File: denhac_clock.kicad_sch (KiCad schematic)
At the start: 54 parts, among them SW1 SET, SW2 CHANGE, U1 SN74HC595N, U2 D_H1, U3 SN74HC595N, U4 D_H1, U5 SN74HC595N, U6 D_M1, U7 SN74HC595N, U8 D_M2, U9 DS1307+, Y1 32.768kHz

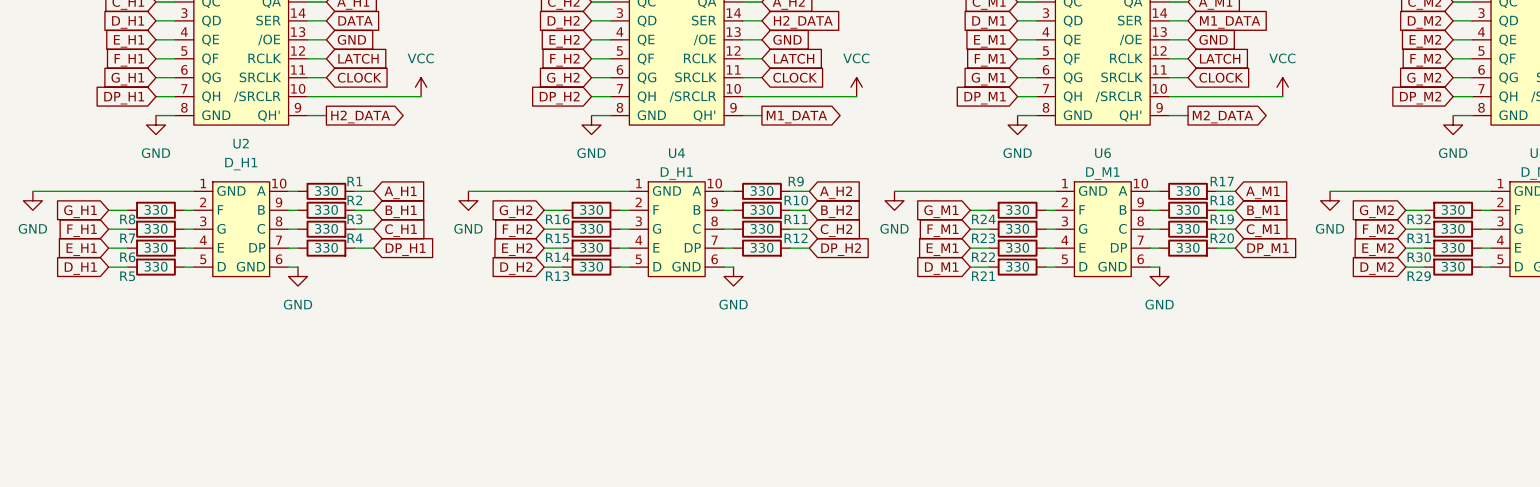
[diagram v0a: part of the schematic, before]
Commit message: rotate D_M1 by 180 degrees so that we can use D_H2 and D_M1 decimal points to create a "colon", and fix pins F and G on all D_ elements"
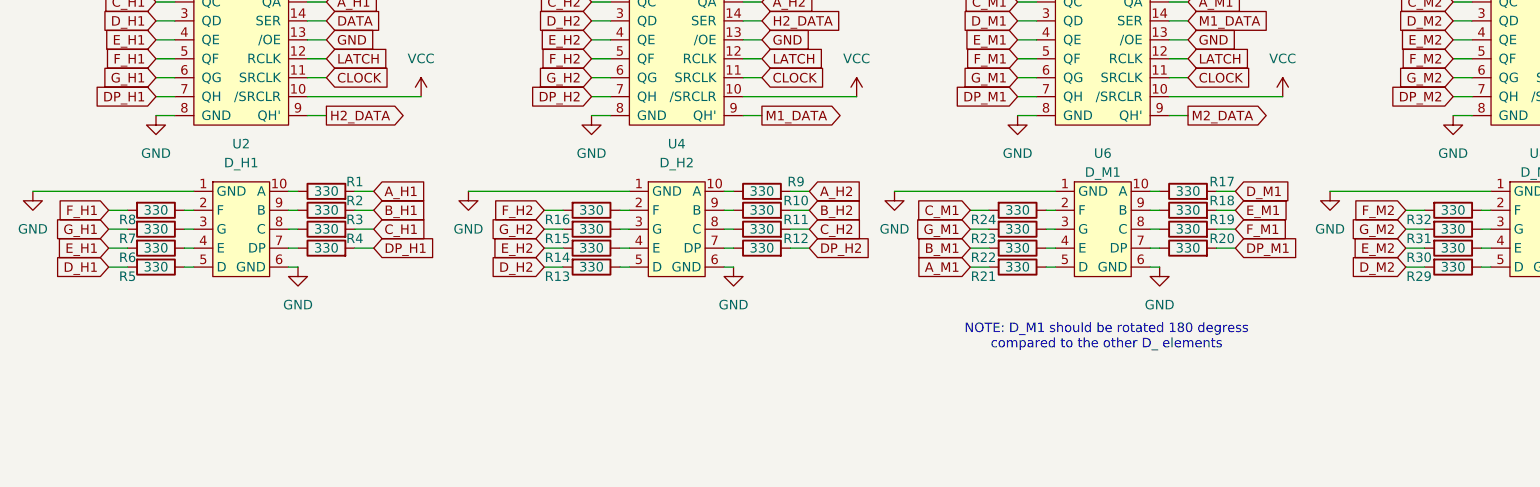
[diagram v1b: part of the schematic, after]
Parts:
- U4: value D_H1 -> D_H2
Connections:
- net A_M1: now also R21.2; no longer R17.2
- net B_M1: now also R22.2; no longer R18.2
- net C_M1: now also R24.2; no longer R19.2
- net D_M1: now also R17.2; no longer R21.2
- net E_M1: now also R18.2; no longer R22.2
- net F_H1: now also R8.2; no longer R7.2
- net F_H2: now also R16.2; no longer R15.2
- net F_M1: now also R19.2; no longer R23.2
- net F_M2: now also R32.2; no longer R31.2
- net G_H1: now also R7.2; no longer R8.2
- net G_H2: now also R15.2; no longer R16.2
- net G_M1: now also R23.2; no longer R24.2
- net G_M2: now also R31.2; no longer R32.2
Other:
- note added: "NOTE: D_M1 should be rotated 180 degress compared to the other D_ elements"
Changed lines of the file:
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@@
 	(generator_version "9.0")
 	(paper "A4")
+	(text "NOTE: D_M1 should be rotated 180 degress\ncompared to the other D_ elements"
+		(exclude_from_sim no)
+		(at 175.768 70.358 0)
+		(effects
+			(font
+				(size 1.27 1.27)
+			)
+		)
+	)
 	(junction
 		(at 62.23 179.07)
@@
 		)
 	)
-	(global_label "D_M1"
+	(global_label "A_M1"
 		(shape input)
 		(at 157.48 60.96 180)
@@
 		)
 		(property "Intersheetrefs" "${INTERSHEET_REFS}"
-			(at 149.5963 60.96 0)
+			(at 149.7777 60.96 0)
 			(effects
 				(font
@@
 		)
 	)
-	(global_label "A_M1"
+	(global_label "D_M1"
 		(shape input)
 		(at 193.04 50.8 0)
@@
 		)
 		(property "Intersheetrefs" "${INTERSHEET_REFS}"
-			(at 200.7423 50.8 0)
+			(at 200.9237 50.8 0)
 			(effects
 				(font
@@
 	(global_label "F_H1"
 		(shape input)
-		(at 41.91 55.88 180)
+		(at 41.91 53.34 180)
 		(fields_autoplaced yes)
 		(effects
@@
 		)
 		(property "Intersheetrefs" "${INTERSHEET_REFS}"
-			(at 34.3286 55.88 0)
+			(at 34.3286 53.34 0)
 			(effects
 				(font
@@
 	(global_label "G_H1"
 		(shape input)
-		(at 41.91 53.34 180)
+		(at 41.91 55.88 180)
 		(fields_autoplaced yes)
 		(effects
@@
 		)
 		(property "Intersheetrefs" "${INTERSHEET_REFS}"
-			(at 34.1472 53.34 0)
+			(at 34.1472 55.88 0)
 			(effects
 				(font
@@
 	(global_label "G_M2"
 		(shape input)
-		(at 215.9 53.34 180)
+		(at 215.9 55.88 180)
 		(fields_autoplaced yes)
 		(effects
@@
 		)
 		(property "Intersheetrefs" "${INTERSHEET_REFS}"
-			(at 208.0163 53.34 0)
+			(at 208.0163 55.88 0)
 			(effects
 				(font
@@
 		)
 	)
-	(global_label "E_M1"
+	(global_label "B_M1"
 		(shape input)
 		(at 157.48 58.42 180)
@@
 		)
 		(property "Intersheetrefs" "${INTERSHEET_REFS}"
-			(at 149.7173 58.42 0)
+			(at 149.5963 58.42 0)
 			(effects
 				(font
@@
 		)
 	)
-	(global_label "B_M1"
+	(global_label "E_M1"
 		(shape input)
 		(at 193.04 53.34 0)
@@
 		)
 		(property "Intersheetrefs" "${INTERSHEET_REFS}"
-			(at 200.9237 53.34 0)
+			(at 200.8027 53.34 0)
 			(effects
 				(font
@@
 	(global_label "F_H2"
 		(shape input)
-		(at 100.33 55.88 180)
+		(at 100.33 53.34 180)
 		(fields_autoplaced yes)
 		(effects
@@
 		)
 		(property "Intersheetrefs" "${INTERSHEET_REFS}"
-			(at 92.7486 55.88 0)
+			(at 92.7486 53.34 0)
 			(effects
 				(font
@@
 	(global_label "G_M1"
 		(shape input)
-		(at 157.48 53.34 180)
+		(at 157.48 55.88 180)
 		(fields_autoplaced yes)
 		(effects
@@
 		)
 		(property "Intersheetrefs" "${INTERSHEET_REFS}"
-			(at 149.5963 53.34 0)
+			(at 149.5963 55.88 0)
 			(effects
 				(font
@@
 	(global_label "G_H2"
 		(shape input)
-		(at 100.33 53.34 180)
+		(at 100.33 55.88 180)
 		(fields_autoplaced yes)
 		(effects
@@
 		)
 		(property "Intersheetrefs" "${INTERSHEET_REFS}"
-			(at 92.5672 53.34 0)
+			(at 92.5672 55.88 0)
 			(effects
 				(font
@@
 		)
 	)
-	(global_label "F_M1"
+	(global_label "C_M1"
 		(shape input)
-		(at 157.48 55.88 180)
+		(at 157.48 53.34 180)
 		(fields_autoplaced yes)
 		(effects
@@
 		)
 		(property "Intersheetrefs" "${INTERSHEET_REFS}"
-			(at 149.7777 55.88 0)
+			(at 149.5963 53.34 0)
 			(effects
 				(font
@@
 	(global_label "F_M2"
 		(shape input)
-		(at 215.9 55.88 180)
+		(at 215.9 53.34 180)
 		(fields_autoplaced yes)
 		(effects
@@
 		)
 		(property "Intersheetrefs" "${INTERSHEET_REFS}"
-			(at 208.1977 55.88 0)
+			(at 208.1977 53.34 0)
 			(effects
 				(font
@@
 		)
 	)
-	(global_label "C_M1"
+	(global_label "F_M1"
 		(shape input)
 		(at 193.04 55.88 0)
@@
 		)
 		(property "Intersheetrefs" "${INTERSHEET_REFS}"
-			(at 200.9237 55.88 0)
+			(at 200.7423 55.88 0)
 			(effects
 				(font
@@
 		(fields_autoplaced yes)
 		(property "Reference" "U4"
-			(at 118.11 45.72 0)
+			(at 118.11 44.45 0)
 			(effects
 				(font
@@
 			)
 		)
-		(property "Value" "D_H1"
-			(at 118.11 48.26 0)
+		(property "Value" "D_H2"
+			(at 118.11 46.99 0)
 			(effects
 				(font
